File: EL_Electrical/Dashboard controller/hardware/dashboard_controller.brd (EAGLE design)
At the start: 69.6 x 48.5 mm, 48 parts, among them IC1 MCP2562-E_SN, IC2 MCP2515-I_SO, J1 22-05-7098-09, Q1 BSS138, Q2 BSS138, Q3 BSS138, Q6 BSS138

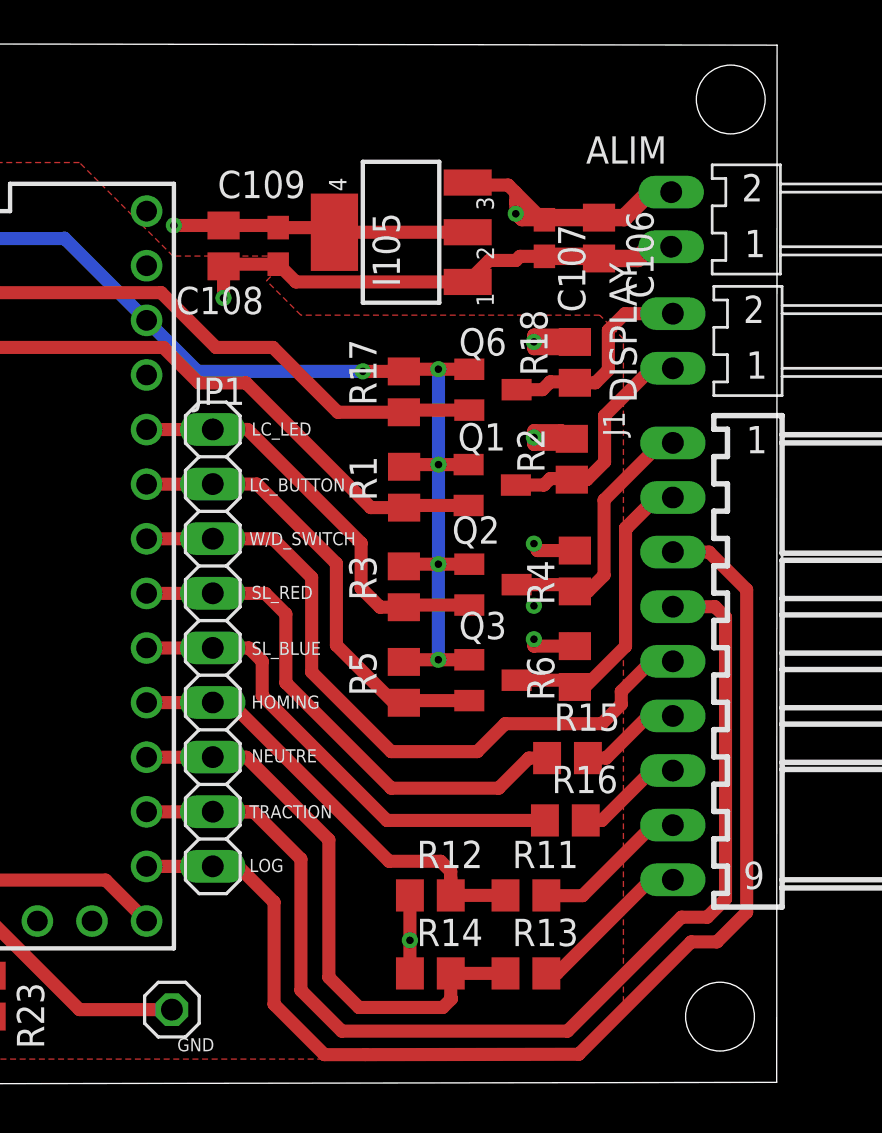
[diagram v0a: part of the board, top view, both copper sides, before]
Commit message: Change circuit to drive the shift LEDs and Launch Control button
TODO: (re)change pin order to shorten 3.3V route (botton layer) and top layers route

TODO 2: add big capacitor
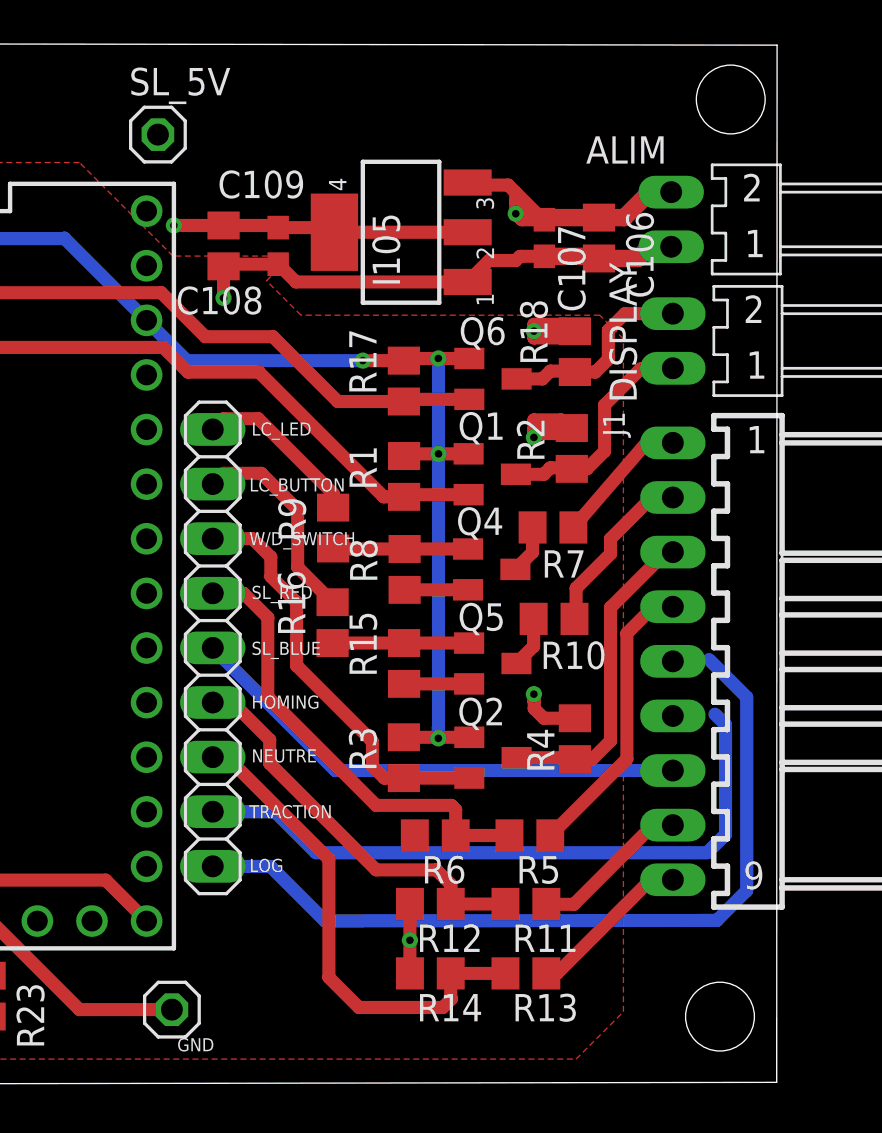
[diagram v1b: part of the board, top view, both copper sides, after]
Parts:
- removed Q3: BSS138, transistor-small-signal:SOT23
- added Q4, Q5: BSS138, transistor-small-signal:SOT23
- added R10, R7: 2k2, rcl:R0805
- added R8: 10k, rcl:R0805
- added R9: 330, rcl:R0805
- added SL_5V: (no value), pinhead:1X01
- R15: value 150 -> 10k
- R16: value 150 -> 330
- R5: value 10k -> 18k
- R6: value 10k -> 6k8
- moved R16 14.2 mm to (49.0, 21.5), turned to 90 degrees
- moved R6 10.2 mm to (53.8, 11.6), turned to 0 degrees
- moved R5 9.22 mm to (58.1, 11.6), turned to 0 degrees
- moved R15 8.78 mm to (52.3, 19.6), turned to 90 degrees
- moved Q2 8.05 mm to (56.4, 15.2)
- moved R3 7.95 mm to (52.3, 15.2)
- moved R4 7.80 mm to (60.2, 16.1)
- moved Q1 0.50 mm to (56.4, 28.4)
- moved Q6 0.50 mm to (56.4, 32.8)
- moved R1 0.50 mm to (52.3, 28.3)
- moved R17 0.50 mm to (52.3, 32.7)
- moved R18 0.50 mm to (60.2, 34.1)
- moved R2 0.50 mm to (60.1, 29.6)
- moved R11 0.40 mm to (58.0, 8.41)
- moved R12 0.40 mm to (53.5, 8.41)
- renumbered JP1 to TEST_PINS
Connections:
- removed net LC_BUTTON: J1.2, Q3.3, R6.1
- removed net N$12: J1.6, R15.2
- removed net N$13: J1.7, R16.2
- new net LC_BUTTON_12V: J1.4, R5.2
- new net N$4: Q4.3, R7.1
- new net N$5: Q5.1, R15.2, R16.1
- new net N$8: Q4.1, R8.2, R9.1
- new net N$9: Q5.3, R10.1
- new net SL_BLUE: J1.2, R10.2
- new net SL_RED: J1.1, R7.2
- net +12V: no longer R6.2
- net +3V3: no longer Q3.1, R5.2
- net +5V: now also SL_5V.1
- net GND: now also Q4.2, Q5.2, R15.1, R6.1, R8.1
- net LC_BUTTON_3.3V: now also R6.2, TEST_PINS.4; no longer Q3.2, TEST_PINS.2
- net LC_LED: now also J1.3; no longer J1.1
- net LC_LED_3.3V: now also TEST_PINS.3; no longer TEST_PINS.1
- net LOG_SWITCH_PIN: now also J1.5; no longer J1.3
- net SL_BLUE_PIN: now also R16.2, TEST_PINS.2; no longer R16.1, TEST_PINS.5
- net SL_RED_PIN: now also R9.2, TEST_PINS.1; no longer R15.1, TEST_PINS.4
- net TC_SWITCH_PIN: now also J1.6; no longer J1.4
- net W/D_SWITCH_PIN: now also J1.7, TEST_PINS.5; no longer J1.5, TEST_PINS.3
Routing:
- net TC_SWITCH_PIN: track 54.9 -> 30.8 mm
- net LOG_SWITCH_PIN: track 60.6 -> 37.9 mm
- net SL_RED_PIN: track 24.8 -> 7.90 mm
- net LC_BUTTON: track 16.4 -> 0.00 mm
- net LC_BUTTON_12V: track 0.00 -> 13.5 mm
- net SL_BLUE_PIN: track 22.8 -> 9.96 mm
- net W/D_SWITCH_PIN: track 33.2 -> 23.8 mm
- net SL_BLUE: track 0.00 -> 8.09 mm
- net SL_RED: track 0.00 -> 6.43 mm
- net N$5: track 0.00 -> 6.35 mm
- net N$8: track 0.00 -> 6.28 mm
- net GND: track 70.8 -> 76.3 mm
- net N$13: track 5.01 -> 0.00 mm
- net N$12: track 4.76 -> 0.00 mm
- net NEUTRE_BUTTON_3.3V: track 26.7 -> 23.1 mm
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
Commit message: Delete LC_LED and change pin order and routes (Dashboard controller)
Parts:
- removed Q2: BSS138, transistor-small-signal:SOT23
- removed R3, R4: 10k, rcl:R0805
- TEST_PINS: device test_pin_DTA:1X09 -> test_pin_DTA:1X08
- moved R5 2.55 mm to (57.6, 14.1)
- moved R6 2.55 mm to (53.2, 14.1)
- moved R11 1.94 mm to (57.7, 10.3)
- moved R12 1.94 mm to (53.3, 10.3)
- moved R13 1.30 mm to (57.7, 6.46)
- moved R14 1.30 mm to (53.3, 6.46)
- moved TEST_PINS 1.29 mm to (43.2, 19.1)
- moved SL_5V 0.74 mm to (40.6, 43.5)
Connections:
- removed net LC_LED: J1.3, Q2.3, R4.1
- removed net LC_LED_3.3V: Q2.2, R3.1, TEST_PINS.3, U$1.22/A8
- net +12V: no longer R4.2
- net +3V3: no longer Q2.1, R3.2
- net +5V: now also J1.1
- net HOMING_BUTTON_3.3V: now also TEST_PINS.7, U$1.15/A1; no longer TEST_PINS.6, U$1.17/A3
- net LC_BUTTON_12V: now also J1.7; no longer J1.4
- net LC_BUTTON_3.3V: now also TEST_PINS.6, U$1.16/A2; no longer TEST_PINS.4, U$1.21/A7
- net LOG_SWITCH_PIN: now also J1.4, TEST_PINS.3, U$1.19/A5; no longer J1.5, TEST_PINS.9, U$1.14/A0
- net NEUTRE_BUTTON_3.3V: now also TEST_PINS.8, U$1.14/A0; no longer TEST_PINS.7, U$1.16/A2
- net SL_BLUE: now also J1.3; no longer J1.2
- net SL_BLUE_PIN: now also U$1.20/A6; no longer U$1.18/A4
- net SL_RED: now also J1.2; no longer J1.1
- net SL_RED_PIN: now also U$1.21/A7; no longer U$1.19/A5
- net TC_SWITCH_PIN: now also J1.5, TEST_PINS.4, U$1.18/A4; no longer J1.6, TEST_PINS.8, U$1.15/A1
- net W/D_SWITCH_PIN: now also J1.6, U$1.17/A3; no longer J1.7, U$1.20/A6
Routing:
- net +12V: track 42.8 -> 15.6 mm, vias 2 -> 0
- net GND: track 76.3 -> 100.2 mm, vias 3 -> 2
- net LC_LED_3.3V: track 19.5 -> 0.00 mm
- net +3V3: track 99.2 -> 82.9 mm, vias 6 -> 5
- net LC_LED: track 14.9 -> 0.00 mm
- net LOG_SWITCH_PIN: track 37.9 -> 24.7 mm
- net LC_BUTTON_12V: track 13.5 -> 6.42 mm
- net TC_SWITCH_PIN: track 30.8 -> 24.7 mm
- net NEUTRE_BUTTON_3.3V: track 23.1 -> 18.1 mm
- net LC_BUTTON_3.3V: track 21.3 -> 18.2 mm, vias 0 -> 1
- net SL_BLUE: track 8.09 -> 5.97 mm
- net +5V: track 106.5 -> 108.5 mm
- net SL_RED_PIN: track 7.90 -> 9.30 mm
- net SL_RED: track 6.43 -> 5.20 mm
- net SL_BLUE_PIN: track 9.96 -> 11.0 mm
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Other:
- board text added: "5V"
- board text added: "LAUNCH"
- board text added: "TC"
- board text added: "W/D"
- board text removed: "LC_BUTTON"
- board text removed: "LC_LED"
- board text removed: "TRACTION"
- board text removed: "W/D_SWITCH"

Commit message: Add capacitors (470uF: about 18,20mm x 10,8mm; Footprint utilisé 25mm x 10mm)
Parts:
- added C2: 1000uF, rcl:E25-10
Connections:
- net +12V: now also C2.+
- net GND: now also C2.-
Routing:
- net +12V: track 15.6 -> 14.6 mm
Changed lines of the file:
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@@
 <attribute name="VALUE" x="40.05" y="29.21" size="1.27" layer="27" rot="R270"/>
+</element>
+<element name="C2" library="rcl" library_urn="urn:adsk.eagle:library:334" package="E25-10" package3d_urn="urn:adsk.eagle:package:23352/1" value="1000uF" x="6.775" y="-9.675" smashed="yes">
+<attribute name="NAME" x="-3.131" y="-4.341" size="1.778" layer="25" ratio="10"/>
+<attribute name="POPULARITY" value="0" x="6.775" y="-9.675" size="1.778" layer="27" display="off"/>
+<attribute name="SPICEPREFIX" value="C" x="6.775" y="-9.675" size="1.778" layer="27" display="off"/>
+<attribute name="VALUE" x="2.7364" y="-12.1642" size="1.778" layer="27" ratio="10"/>
 </element>
 </elements>
@@
 <contactref element="C107" pad="1"/>
 <contactref element="C106" pad="1"/>
-<contactref element="ALIM" pad="2"/>
-<wire x1="64.7225" y1="41.5225" x2="63.7225" y2="41.5225" width="0.8128" layer="1"/>
 <wire x1="63.7225" y1="41.5225" x2="62.5375" y2="40.3375" width="0.8128" layer="1"/>
 <wire x1="62.5375" y1="40.3375" x2="61.365" y2="40.3375" width="0.8128" layer="1"/>
@@
 <wire x1="58.825" y1="40.2375" x2="57.7732" y2="40.2375" width="0.6096" layer="1"/>
 <wire x1="57.7732" y1="40.2375" x2="57.6732" y2="40.3375" width="0.6096" layer="1"/>
-<wire x1="58.825" y1="40.2375" x2="57.5" y2="40.5107" width="0" layer="19" extent="1-15"/>
+<contactref element="C2" pad="+"/>
+<contactref element="ALIM" pad="2"/>
+<wire x1="63.7225" y1="41.5225" x2="64.7225" y2="41.5225" width="0" layer="19" extent="1-1"/>
+<wire x1="57.5" y1="40.5107" x2="58.825" y2="40.2375" width="0" layer="19" extent="1-15"/>
+<wire x1="-5.925" y1="-9.675" x2="55.2563" y2="41.9689" width="0" layer="19" extent="1-1"/>
 </signal>
 <signal name="+3V3">
@@
 <wire x1="25.0825" y1="40.64" x2="23.27" y2="40.64" width="0.6096" layer="1"/>
 <wire x1="23.27" y1="40.64" x2="22.975" y2="40.935" width="0.6096" layer="1"/>
+<contactref element="C2" pad="-"/>
 <wire x1="55.275" y1="23.025" x2="55.2563" y2="37.3461" width="0" layer="19" extent="1-1"/>
 <wire x1="55.325" y1="18.65" x2="55.275" y2="23.025" width="0" layer="19" extent="1-1"/>
@@
 <wire x1="20.3225" y1="17.4625" x2="32.7025" y2="7.62" width="0" layer="19" extent="1-1"/>
 <wire x1="15.6" y1="27" x2="20.3225" y2="20.32" width="0" layer="19" extent="1-1"/>
-<wire x1="15.875" y1="32.7175" x2="11.9975" y2="40.9325" width="0" layer="19" extent="1-1"/>
+<wire x1="11.9975" y1="40.9325" x2="15.875" y2="32.7175" width="0" layer="19" extent="1-1"/>
 <wire x1="6.985" y1="10.475" x2="20.3225" y2="17.4625" width="0" layer="19" extent="1-1"/>
+<wire x1="19.475" y1="-9.675" x2="29.6025" y2="2.8575" width="0" layer="19" extent="1-1"/>
 </signal>
 <signal name="+5V">

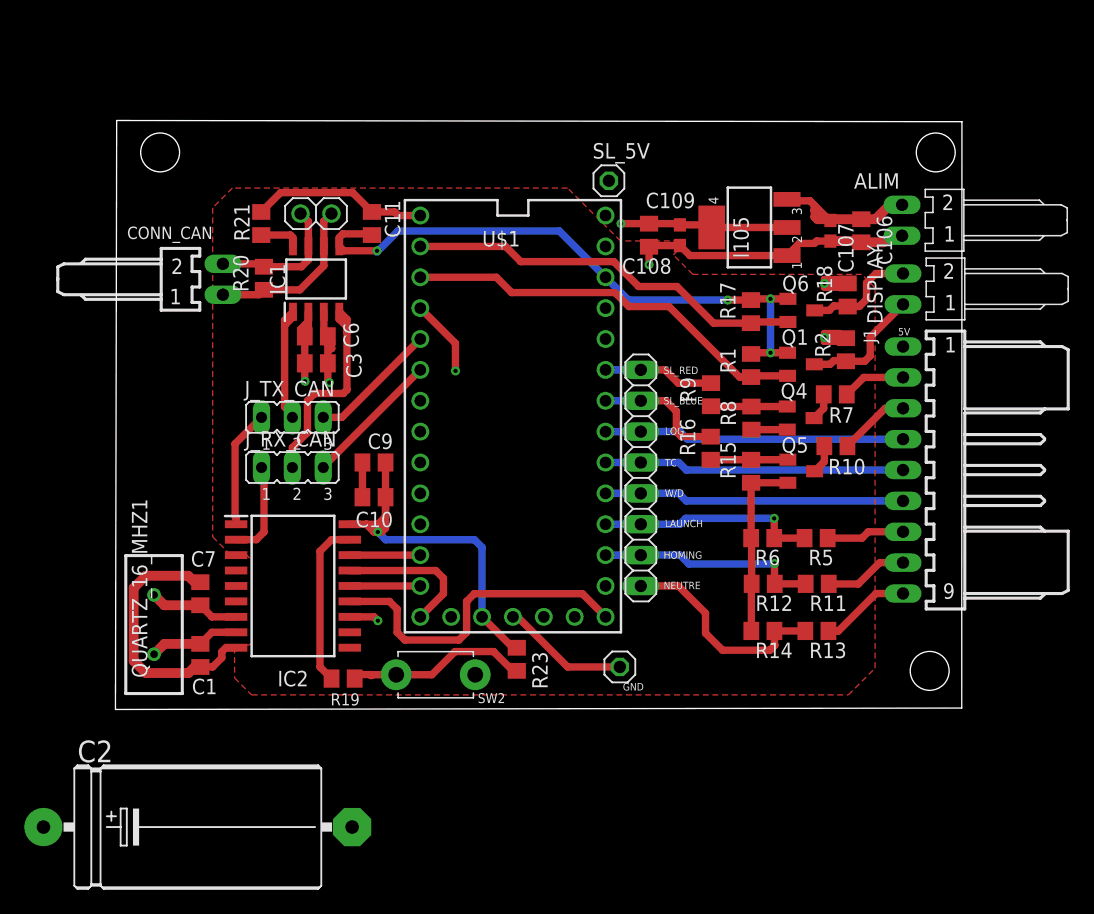
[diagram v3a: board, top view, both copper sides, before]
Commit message: Delete useless resistors (Dashboard_controller)
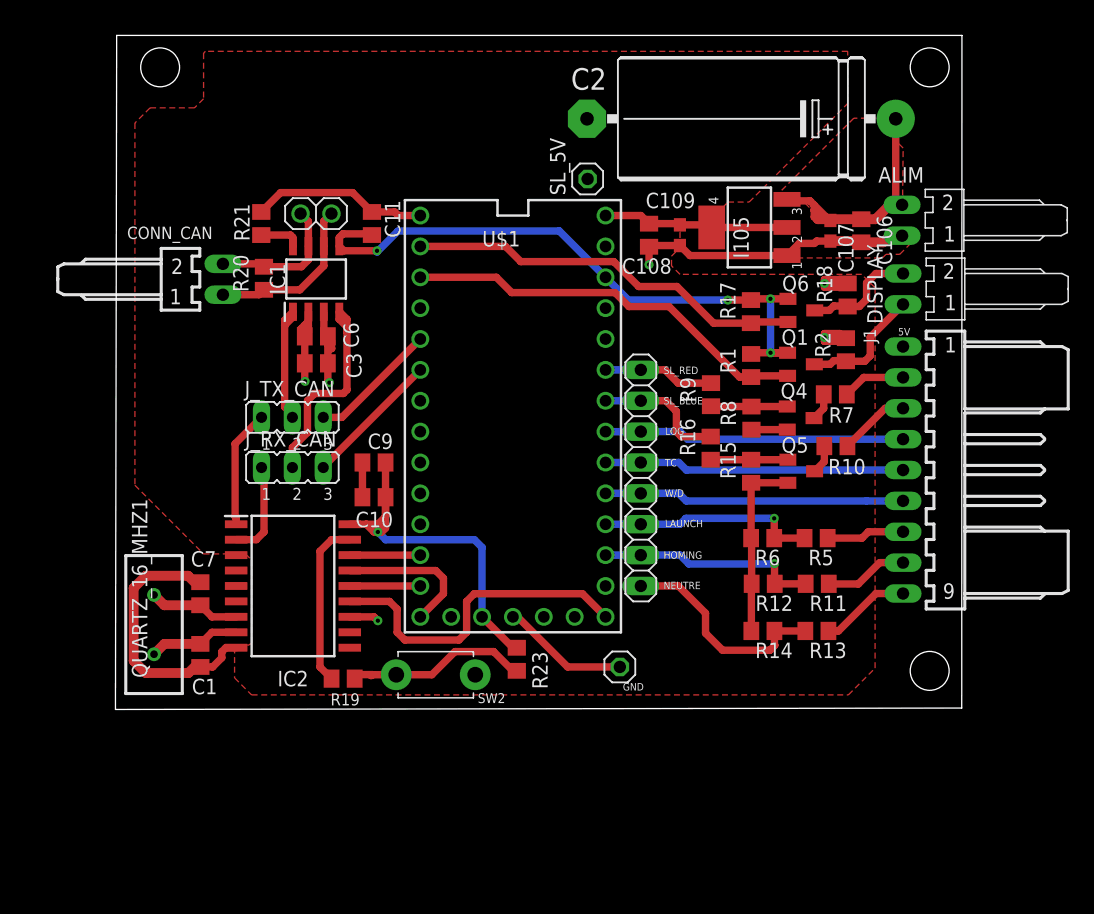
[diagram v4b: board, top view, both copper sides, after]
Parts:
- moved C2 73.5 mm to (51.5, 48.6), turned to 180 degrees
- moved SL_5V 1.76 mm to (38.9, 43.6), turned to 90 degrees
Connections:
- removed net GEAR_POT: U$1.RESET/DAC
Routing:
- net +5V: track 108.5 -> 121.1 mm, vias 4 -> 3
- net +12V: track 14.6 -> 21.6 mm
- net +3V3: track 82.9 -> 84.3 mm
- net INT: vias 2 -> 1
- added copper zone on layer 1, net +12V
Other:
- board size 69.6 x 48.5 mm -> 69.6 x 55.5 mm

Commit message: Delete useless resistors (Dashboard_controller)
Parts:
- removed R11, R13, R5: 18k, rcl:R0805
- removed R12, R14, R6: 6k8, rcl:R0805
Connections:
- removed net HOMING_BUTTON_12V: J1.8, R11.2
- removed net HOMING_BUTTON_3.3V: R11.1, R12.2, TEST_PINS.7, U$1.15/A1
- removed net LC_BUTTON_12V: J1.7, R5.2
- removed net LC_BUTTON_3.3V: R5.1, R6.2, TEST_PINS.6, U$1.16/A2
- removed net NEUTRE_BUTTON_12V: J1.9, R13.2
- removed net NEUTRE_BUTTON_3.3V: R13.1, R14.2, TEST_PINS.8, U$1.14/A0
- new net HOMING_BUTTON: J1.8, TEST_PINS.7, U$1.15/A1
- new net LC_BUTTON: J1.7, TEST_PINS.6, U$1.16/A2
- new net NEUTRE_BUTTON: J1.9, TEST_PINS.8, U$1.14/A0
- net GND: no longer R12.1, R14.1, R6.1
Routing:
- net LC_BUTTON: track 0.00 -> 24.7 mm
- net NEUTRE_BUTTON: track 0.00 -> 24.7 mm
- net HOMING_BUTTON: track 0.00 -> 24.7 mm
- net HOMING_BUTTON_3.3V: track 18.4 -> 0.00 mm, vias 1 -> 0
- net LC_BUTTON_3.3V: track 18.2 -> 0.00 mm, vias 1 -> 0
- net NEUTRE_BUTTON_3.3V: track 18.1 -> 0.00 mm
- net GND: track 100.2 -> 88.0 mm
- net NEUTRE_BUTTON_12V: track 7.91 -> 0.00 mm
- net HOMING_BUTTON_12V: track 6.84 -> 0.00 mm
- net LC_BUTTON_12V: track 6.42 -> 0.00 mm
